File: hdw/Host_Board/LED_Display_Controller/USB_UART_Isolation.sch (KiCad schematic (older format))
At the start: 8 parts

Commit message: I said never do this, it's bad for you
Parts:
- added R? (x4): 100, symbol LED_Display_Local_Library:R_Custom
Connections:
- net USB_UART_RX: now also R?.1; no longer R?.2, U?.2 (OUTA)
- net USB_UART_RX_ISO: now also R?.1; no longer R?.2, U?.7 (INA)
- net USB_UART_TX: now also R?.1; no longer R?.2, U?.3 (INB)
- net USB_UART_TX_ISO: now also R?.1; no longer R?.2, U?.6 (OUTB)
- new net: R?.2, R?.2, U?.2 (OUTA)
- new net: R?.2, R?.2, U?.3 (INB)
- new net: R?.2, R?.2, U?.6 (OUTB)
- new net: R?.2, R?.2, U?.7 (INA)
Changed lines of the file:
@@
 $Descr A 11000 8500
 encoding utf-8
-Sheet 6 32
+Sheet 6 31
 Title ""
 Date ""
@@
 Comment4 ""
 $EndDescr
-Text GLabel 2850 3470 0    50   Output ~ 0
+Text GLabel 2550 3470 0    50   Output ~ 0
 USB_UART_RX
-Text GLabel 2850 3570 0    50   Input ~ 0
+Text GLabel 2550 3570 0    50   Input ~ 0
 USB_UART_TX
-Text GLabel 8310 3470 2    50   Input ~ 0
+Text GLabel 8610 3470 2    50   Input ~ 0
 USB_UART_RX_ISO
-Text GLabel 8330 3570 2    50   Output ~ 0
+Text GLabel 8610 3570 2    50   Output ~ 0
 USB_UART_TX_ISO
 $Comp
@@
 Connection ~ 6900 3570
 Wire Wire Line
-	6900 3570 8330 3570
+	6900 3570 8310 3570
 Wire Wire Line
 	7530 3180 7530 3470
@@
 Wire Wire Line
 	7530 3470 8310 3470
+$Comp
+L LED_Display_Local_Library:R_Custom R?
+U 1 1 5BE39290
+P 2700 3470
+AR Path="/5BAAE2B6/5BE39290" Ref="R?"  Part="1"
+AR Path="/5BB6CF6D/5BE39290" Ref="R?"  Part="1"
+AR Path="/5BBE424C/5BE39290" Ref="R?"  Part="1"
+AR Path="/5BAAE1DC/5BE39290" Ref="R?"  Part="1"
+F 0 "R?" V 2660 3330 50  0000 R CNN
+F 1 "100" V 2700 3470 50  0000 C CNN
+F 2 "" H 2700 3470 50  0001 C CNN
+F 3 "" H 2700 3470 50  0001 C CNN
+F 4 "0603" V 2800 3470 50  0001 C CNN "display_footprint"
+F 5 "1%" V 2900 3470 50  0001 C CNN "Tolerance"
+F 6 "1/10W" V 3000 3470 50  0001 C CNN "Wattage"
+F 7 "PN" H 3000 3870 60  0001 C CNN "Digi-Key PN"
+	1    2700 3470
+	0    -1   1    0
+$EndComp
+$Comp
+L LED_Display_Local_Library:R_Custom R?
+U 1 1 5BE3929B
+P 2700 3570
+AR Path="/5BAAE2B6/5BE3929B" Ref="R?"  Part="1"
+AR Path="/5BB6CF6D/5BE3929B" Ref="R?"  Part="1"
+AR Path="/5BBE424C/5BE3929B" Ref="R?"  Part="1"
+AR Path="/5BAAE1DC/5BE3929B" Ref="R?"  Part="1"
+F 0 "R?" V 2660 3430 50  0000 R CNN
+F 1 "100" V 2700 3570 50  0000 C CNN
+F 2 "" H 2700 3570 50  0001 C CNN
+F 3 "" H 2700 3570 50  0001 C CNN
+F 4 "0603" V 2800 3570 50  0001 C CNN "display_footprint"
+F 5 "1%" V 2900 3570 50  0001 C CNN "Tolerance"
+F 6 "1/10W" V 3000 3570 50  0001 C CNN "Wattage"
+F 7 "PN" H 3000 3970 60  0001 C CNN "Digi-Key PN"
+	1    2700 3570
+	0    -1   1    0
+$EndComp
+$Comp
+L LED_Display_Local_Library:R_Custom R?
+U 1 1 5BE39F31
+P 8460 3470
+AR Path="/5BAAE2B6/5BE39F31" Ref="R?"  Part="1"
+AR Path="/5BB6CF6D/5BE39F31" Ref="R?"  Part="1"
+AR Path="/5BBE424C/5BE39F31" Ref="R?"  Part="1"
+AR Path="/5BAAE1DC/5BE39F31" Ref="R?"  Part="1"
+F 0 "R?" V 8420 3330 50  0000 R CNN
+F 1 "100" V 8460 3470 50  0000 C CNN
+F 2 "" H 8460 3470 50  0001 C CNN
+F 3 "" H 8460 3470 50  0001 C CNN
+F 4 "0603" V 8560 3470 50  0001 C CNN "display_footprint"
+F 5 "1%" V 8660 3470 50  0001 C CNN "Tolerance"
+F 6 "1/10W" V 8760 3470 50  0001 C CNN "Wattage"
+F 7 "PN" H 8760 3870 60  0001 C CNN "Digi-Key PN"
+	1    8460 3470
+	0    1    1    0
+$EndComp
+$Comp
+L LED_Display_Local_Library:R_Custom R?
+U 1 1 5BE39F3C
+P 8460 3570
+AR Path="/5BAAE2B6/5BE39F3C" Ref="R?"  Part="1"
+AR Path="/5BB6CF6D/5BE39F3C" Ref="R?"  Part="1"
+AR Path="/5BBE424C/5BE39F3C" Ref="R?"  Part="1"
+AR Path="/5BAAE1DC/5BE39F3C" Ref="R?"  Part="1"
+F 0 "R?" V 8420 3430 50  0000 R CNN
+F 1 "100" V 8460 3570 50  0000 C CNN
+F 2 "" H 8460 3570 50  0001 C CNN
+F 3 "" H 8460 3570 50  0001 C CNN
+F 4 "0603" V 8560 3570 50  0001 C CNN "display_footprint"
+F 5 "1%" V 8660 3570 50  0001 C CNN "Tolerance"
+F 6 "1/10W" V 8760 3570 50  0001 C CNN "Wattage"
+F 7 "PN" H 8760 3970 60  0001 C CNN "Digi-Key PN"
+	1    8460 3570
+	0    1    1    0
+$EndComp
 $EndSCHEMATC

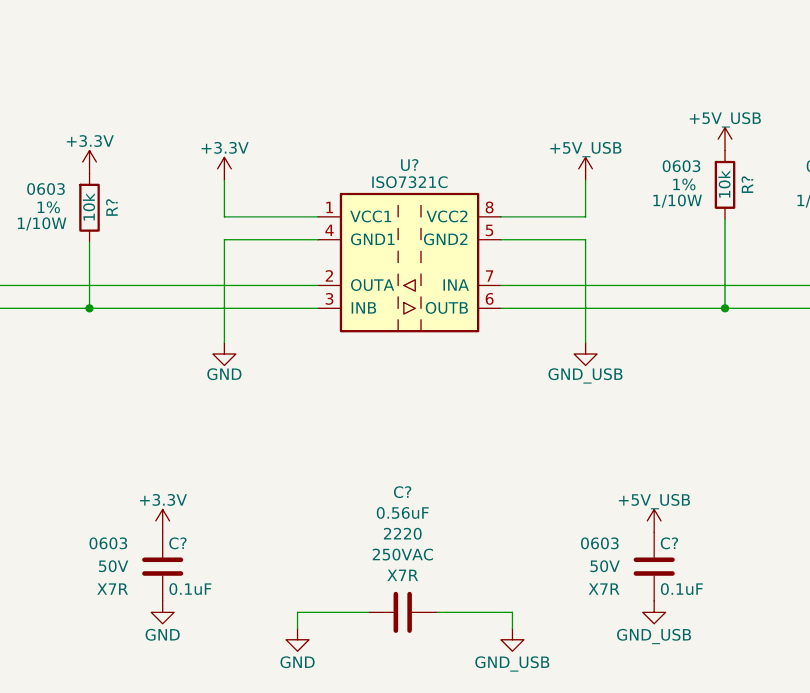
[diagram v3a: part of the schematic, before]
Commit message: Added graphical symbols to certain sheets
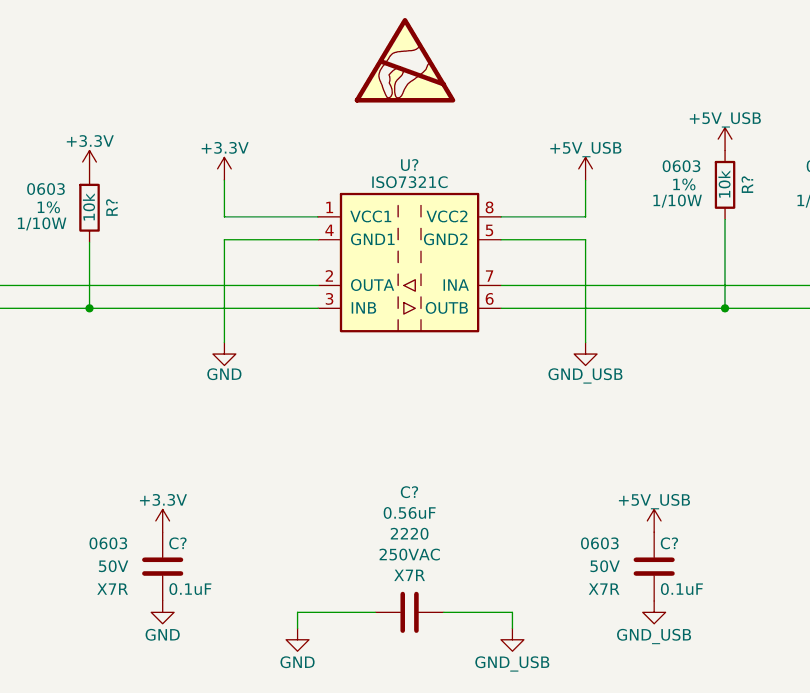
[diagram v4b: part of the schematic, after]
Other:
- moved on the sheet: C?
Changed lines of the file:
@@
 L LED_Display_Local_Library:C_Custom C?
 U 1 1 5BB19187
-P 5490 4900
-F 0 "C?" V 6014 4900 50  0000 C CNN
-F 1 "0.56uF" V 5923 4900 50  0000 C CNN
-F 2 "" H 5528 4750 50  0001 C CNN
-F 3 "" H 5515 5000 50  0001 C CNN
-F 4 "PN" H 5915 5400 60  0001 C CNN "Digi-Key PN"
-F 5 "2220" V 5832 4900 50  0000 C CNN "display_footprint"
-F 6 "250VAC" V 5741 4900 50  0000 C CNN "Voltage"
-F 7 "X7R" V 5650 4900 50  0000 C CNN "Dielectric"
-	1    5490 4900
+P 5520 4900
+F 0 "C?" V 6044 4900 50  0000 C CNN
+F 1 "0.56uF" V 5953 4900 50  0000 C CNN
+F 2 "" H 5558 4750 50  0001 C CNN
+F 3 "" H 5545 5000 50  0001 C CNN
+F 4 "PN" H 5945 5400 60  0001 C CNN "Digi-Key PN"
+F 5 "2220" V 5862 4900 50  0000 C CNN "display_footprint"
+F 6 "250VAC" V 5771 4900 50  0000 C CNN "Voltage"
+F 7 "X7R" V 5680 4900 50  0000 C CNN "Dielectric"
+	1    5520 4900
 	0    -1   -1   0
 $EndComp
@@
 	5030 4970 5030 4900
 Wire Wire Line
-	5030 4900 5340 4900
-Wire Wire Line
-	5640 4900 5970 4900
+	5030 4900 5370 4900
+Wire Wire Line
+	5670 4900 5970 4900
 Wire Wire Line
 	5970 4900 5970 4970
@@
 	0    1    1    0
 $EndComp
+$Comp
+L Graphic:SYM_ESD_Large #SYM?
+U 1 1 5C005A48
+P 5500 2460
+AR Path="/5BAAE0FA/5C005A48" Ref="#SYM?"  Part="1"
+AR Path="/5BAAE1DC/5C005A48" Ref="#SYM?"  Part="1"
+F 0 "#SYM?" H 5500 2660 50  0001 C CNN
+F 1 "SYM_ESD_Large" H 5500 2210 50  0001 C CNN
+F 2 "" H 5495 2430 50  0001 C CNN
+F 3 "~" H 5495 2430 50  0001 C CNN
+	1    5500 2460
+	1    0    0    -1
+$EndComp
 $EndSCHEMATC

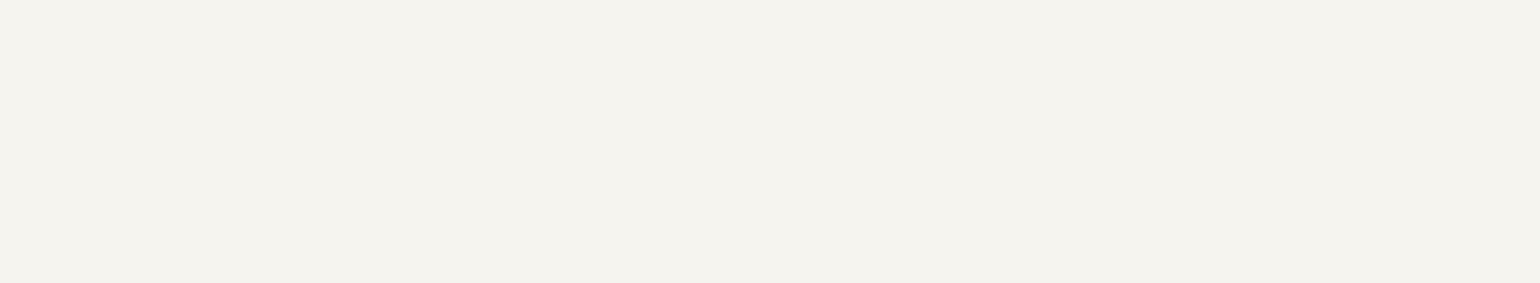
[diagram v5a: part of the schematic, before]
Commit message: Added titles and MU logo to each sheet
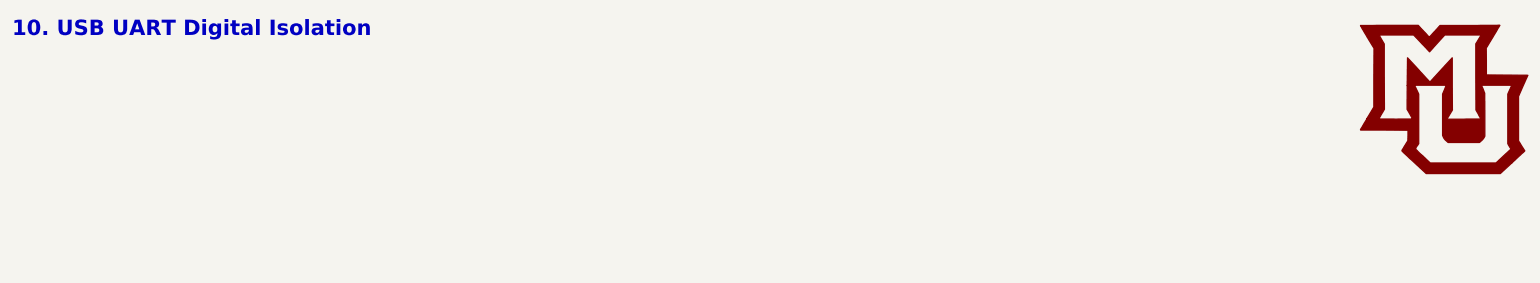
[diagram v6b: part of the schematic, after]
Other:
- note added: "10. USB UART Digital Isolation"
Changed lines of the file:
@@
+	1    0    0    -1
+$EndComp
+Text Notes 550  700  0    100  ~ 20
+10. USB UART Digital Isolation
+$Comp
+L LED_Display_Local_Library:MU_Logo #G?
+U 1 1 5BFF3086
+P 9900 1100
+F 0 "#G?" H 9900 614 60  0001 C CNN
+F 1 "MU_Logo" H 9900 1586 60  0001 C CNN
+F 2 "" H 9900 1100 50  0001 C CNN
+F 3 "" H 9900 1100 50  0001 C CNN
+	1    9900 1100
 	1    0    0    -1
 $EndComp
